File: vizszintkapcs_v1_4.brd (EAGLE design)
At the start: 235.7 x 107.2 mm, 95 parts, among them IC1 UA78M08DCY, IC2 7815TV, U1 MCP3004-I/ST

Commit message: smaller version with danger sign and good holes
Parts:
- moved WL4:OK3 34.8 mm to (159.8, 34.2)
- moved WL6:OK3 34.8 mm to (142.0, 34.2)
- moved WL3:OK3 34.8 mm to (168.7, 34.2)
- moved WL3:R9 34.8 mm to (167.4, 44.3)
- moved WL4:R9 34.8 mm to (158.6, 44.3)
- moved WL5:OK3 34.8 mm to (150.9, 34.2)
- moved WL5:R9 34.8 mm to (149.7, 44.3)
- moved WL6:R9 34.8 mm to (140.8, 44.3)
- moved WL4:R8 33.6 mm to (159.7, 26.8), turned to 0 degrees
- moved WL3:R8 33.6 mm to (168.6, 26.8), turned to 0 degrees
- moved WL5:R8 33.6 mm to (150.8, 26.8), turned to 0 degrees
- moved WL6:R8 33.6 mm to (141.9, 26.8), turned to 0 degrees
- moved U$6 33.0 mm to (165.1, 5.08)
- moved WL4:B3 32.1 mm to (159.7, 16.5)
- moved WL4:C4 32.1 mm to (159.7, 24.1)
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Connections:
- net 230V0: now also U$8.P$3@1, U$8.P$3@2; no longer U$8.P$3
- net 230VPHASE: now also U$8.P$1@1, U$8.P$1@2; no longer U$8.P$1
- net COMMON_EARTH: now also U$8.P$10@1, U$8.P$10@2, U$8.P$2@1, U$8.P$2@2, U$8.P$5@1, U$8.P$5@2, U$8.P$8@1, U$8.P$8@2; no longer U$8.P$10, U$8.P$2, U$8.P$5, U$8.P$8
- net MOTOR_IN: now also U$8.P$4@1, U$8.P$4@2; no longer U$8.P$4
- net MOTOR_IN_2: now also U$8.P$7@1, U$8.P$7@2; no longer U$8.P$7
- net MOTOR_OUT_1: now also U$8.P$6@1, U$8.P$6@2; no longer U$8.P$6
- net MOTOR_OUT_2: now also U$8.P$9@1, U$8.P$9@2; no longer U$8.P$9
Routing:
- net DC5V: track 415.8 -> 381.8 mm, vias 7 -> 6
- net MOTOR_IN: track 36.2 -> 66.4 mm
- net MOTOR_OUT_1: track 45.3 -> 73.4 mm
- net P1.6: track 86.9 -> 113.4 mm, vias 1 -> 4
- net MOTOR_IN_2: track 31.9 -> 58.3 mm
- net AC12V: track 114.4 -> 138.7 mm
- net DC15V: track 234.8 -> 212.1 mm
- net COMMON_EARTH: track 52.5 -> 73.6 mm
- net MOTOR_DIRECT_1: track 126.1 -> 108.4 mm
- net P6.1: track 115.9 -> 98.7 mm
- net DC8V: track 126.4 -> 142.0 mm, vias 3 -> 1
- net MOTOR_DIRECT_2: track 152.7 -> 138.5 mm
- net P6.0: track 138.9 -> 125.3 mm
- net 230V0: track 106.2 -> 117.5 mm, vias 1 -> 0
- net P2.7: track 161.4 -> 151.8 mm
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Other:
- board size 235.7 x 107.2 mm -> 197.6 x 97 mm
- board text added: "DANGER! HIGH VOLTAGE!"
- board text added: "High voltage"
- board text added: "Water Cleaning Management System (c) ujoimro, 2015-05-11 https://github.com/ViktorVaczi90/viztisztito"

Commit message: save
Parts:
- B2, B7: device rectifier:RB1A -> rectifier:1KAB
- C1, C10, C13, C2, C3, C5: device capacitor-wima:C2.5-3 -> adafruit:E3,5-8
- IC1: value UA78M08DCY -> UA78M33DCY
- moved C4 5.08 mm to (175.6, 57.0)
- moved C2 4.14 mm to (149.5, 51.1), turned to 270 degrees
- moved C10 3.81 mm to (145.8, 78.7)
- moved C1 2.54 mm to (170.2, 57.1)
- moved C3 2.54 mm to (149.9, 59.7)
- moved B2 2.54 mm to (132.1, 73.7), turned to 180 degrees
- moved C6 2.54 mm to (172.7, 71.1)
- moved C7 2.54 mm to (154.9, 54.6)
- moved C9 2.54 mm to (155.0, 59.8)
- moved IC2 2.54 mm to (154.9, 73.7)
- moved C12 1.27 mm to (140.5, 75.0)
- moved C5 1.27 mm to (166.4, 71.1)
- moved IC1 1.27 mm to (161.3, 55.9)
- moved U$2 1.27 mm to (161.3, 73.7)
- moved C14 1.21 mm to (140.5, 69.8), turned to 90 degrees
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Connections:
- net DC15V: now also C13.+; no longer C13.1
- net DC3.3V: now also C1.+; no longer C1.1
- net DC5V: now also C3.+; no longer C3.1
- net DC8V: now also C5.+; no longer C5.1
- net GND: now also C1.-, C10.-, C13.-, C2.-, C3.-, C5.-; no longer C1.2, C10.2, C13.2, C2.2, C3.2, C5.2
- net REC12V: now also C2.+; no longer C2.1
- net REC24V: now also C10.+; no longer C10.1
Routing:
- net REC24V: track 27.7 -> 38.2 mm
- net GND: track 164.6 -> 154.4 mm
- net REC12V: track 28.1 -> 35.8 mm
- net DC8V: track 142.0 -> 144.8 mm
- net TRANS_OUT: track 170.9 -> 168.3 mm, vias 2 -> 3
- net DC15V: track 212.1 -> 214.1 mm
- net DC5V: track 381.8 -> 380.0 mm
- net AC24V: track 25.3 -> 23.5 mm
- net DC3.3V: track 74.6 -> 76.1 mm

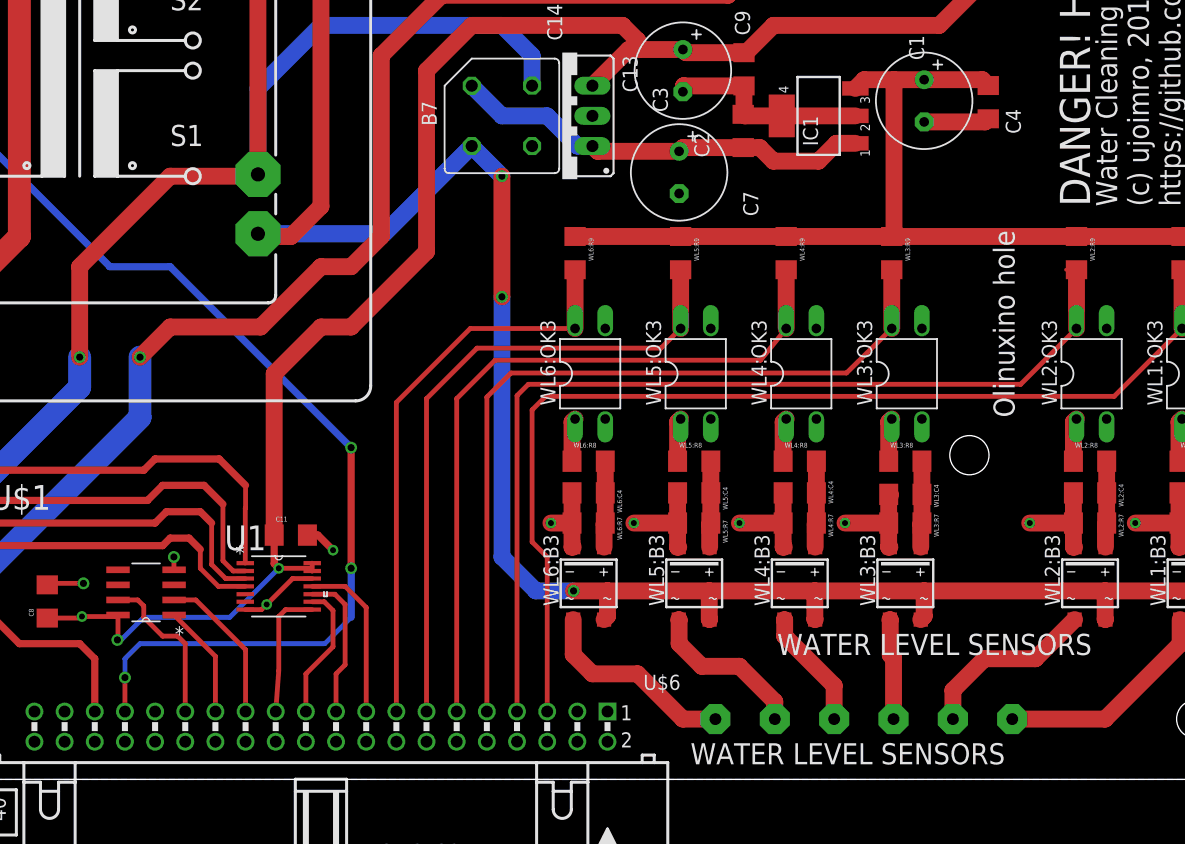
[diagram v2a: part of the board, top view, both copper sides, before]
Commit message: only 4 water level sensor on one board
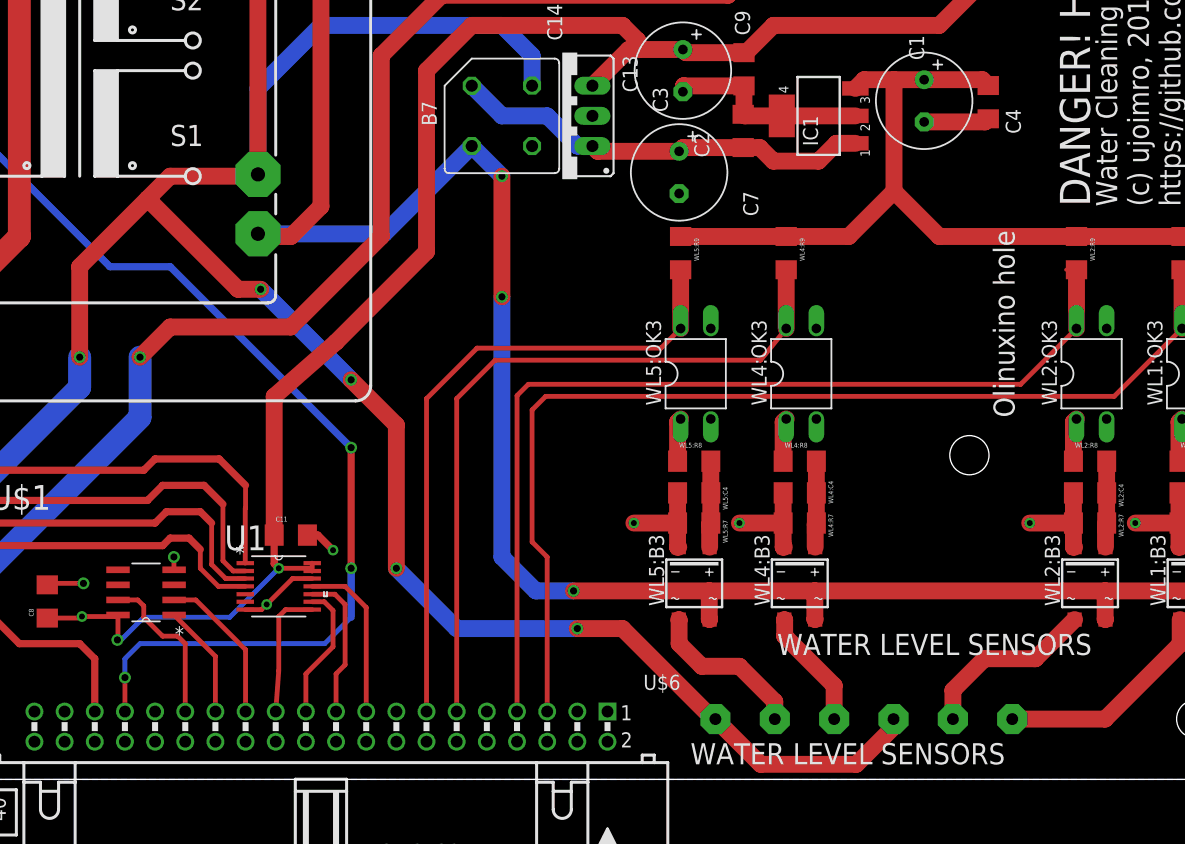
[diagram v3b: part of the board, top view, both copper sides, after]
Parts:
- removed WL3:B3, WL6:B3: MB6S, rectifier:SOIC-4
- removed WL3:C4, WL6:C4: 10uF, SparkFun-Passives:1206
- removed WL3:OK3, WL6:OK3: PC817, optocoupler:DIL04
- removed WL3:R7, WL6:R7: 20k, SparkFun-Resistors:1206
- removed WL3:R8, WL3:R9, WL6:R8, WL6:R9: 2k, SparkFun-Resistors:1206
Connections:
- removed net 3_WATER_IN: U$6.P$3, WL3:B3.~1
- removed net 6_WATER_IN: U$6.P$6, WL6:B3.~1
- removed net WL3:N$12: WL3:B3.+, WL3:C4.1, WL3:R7.2, WL3:R8.2
- removed net WL3:N$13: WL3:OK3.1, WL3:R8.1
- removed net WL6:N$12: WL6:B3.+, WL6:C4.1, WL6:R7.2, WL6:R8.2
- removed net WL6:N$13: WL6:OK3.1, WL6:R8.1
- net AC12V: now also U$6.P$3, U$6.P$6
- net DC3.3V: no longer WL3:R9.1, WL6:R9.1
- net GND: no longer WL3:B3.-, WL3:C4.2, WL3:OK3.2, WL3:OK3.3, WL3:R7.1, WL6:B3.-, WL6:C4.2, WL6:OK3.2, WL6:OK3.3, WL6:R7.1
- net P1.4: no longer WL3:OK3.4, WL3:R9.2
- net P2.5: no longer WL6:OK3.4, WL6:R9.2
- net TRANS_OUT: no longer WL3:B3.~2, WL6:B3.~2
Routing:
- net AC12V: track 138.7 -> 230.3 mm, vias 1 -> 5
- net P1.4: track 67.9 -> 0.00 mm
- net P2.5: track 48.6 -> 0.00 mm
- net 6_WATER_IN: track 17.2 -> 0.00 mm
- net GND: track 154.4 -> 139.5 mm, vias 16 -> 14
- net DC3.3V: track 76.1 -> 66.5 mm
- net 3_WATER_IN: track 8.51 -> 0.00 mm
- net WL3:N$12: track 7.28 -> 0.00 mm
- net WL6:N$12: track 7.28 -> 0.00 mm
- net TRANS_OUT: track 168.3 -> 163.3 mm
- net WL6:N$13: track 3.66 -> 0.00 mm
- net WL3:N$13: track 3.66 -> 0.00 mm
- net DC5V: track 380.0 -> 378.7 mm

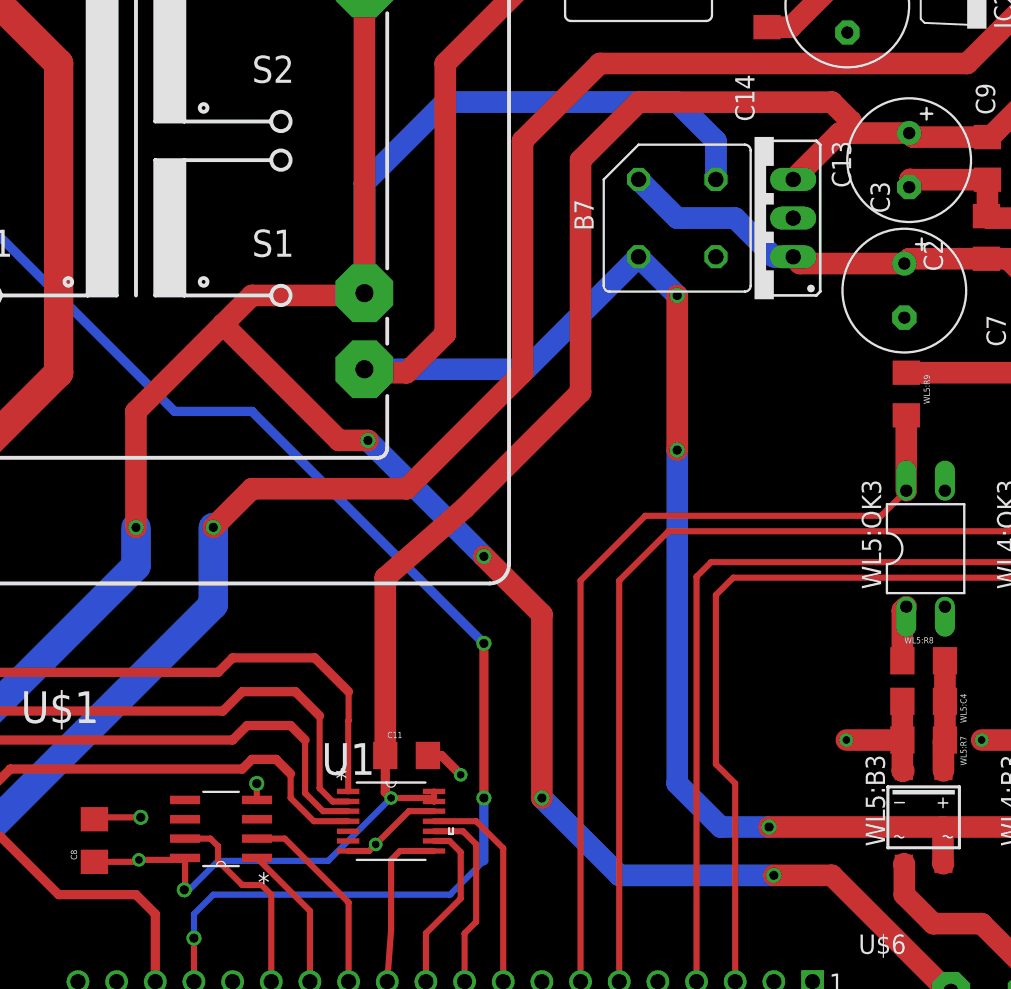
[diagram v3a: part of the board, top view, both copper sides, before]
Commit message: 3.3v spi levels
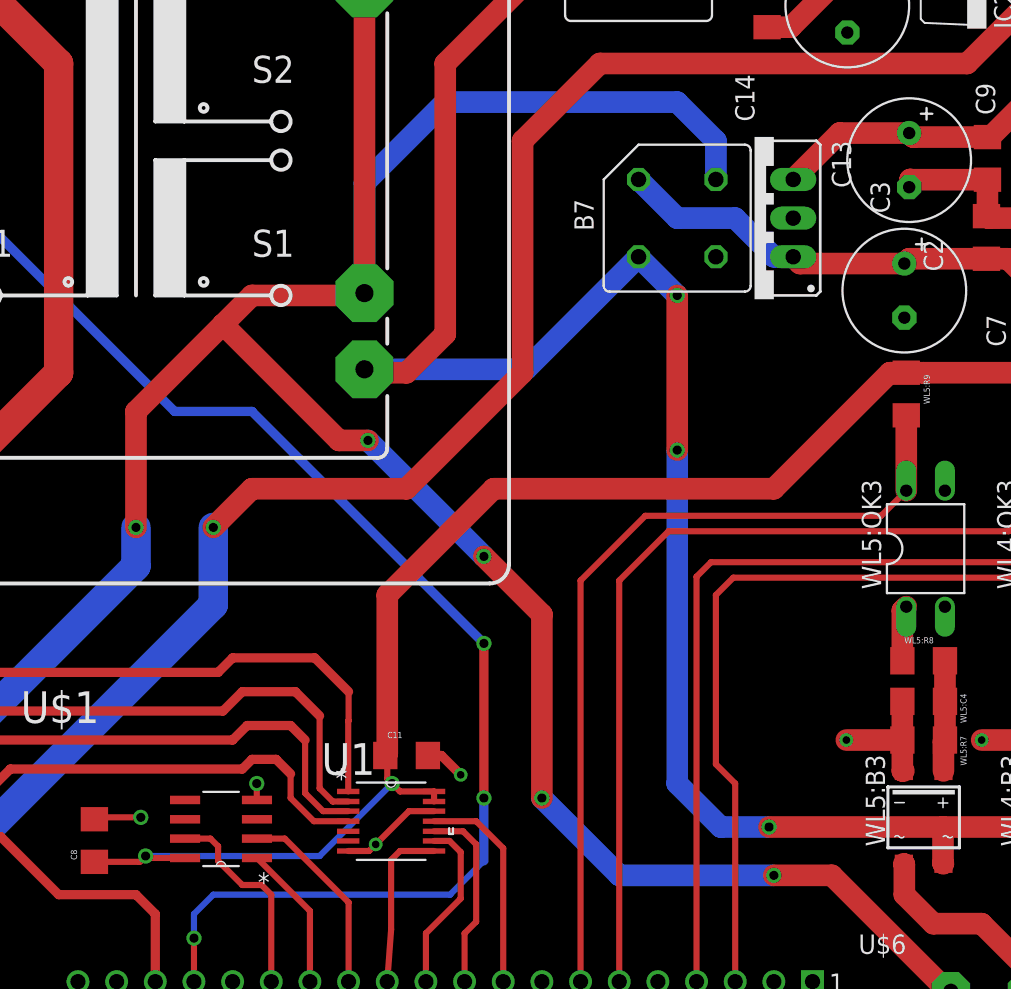
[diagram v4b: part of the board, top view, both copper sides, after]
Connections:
- net DC3.3V: now also C11.1, C8.1, U$1.8, U1.13, U1.14
- net DC5V: no longer C11.1, C8.1, U$1.8, U1.13, U1.14
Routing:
- net DC5V: track 378.7 -> 282.6 mm, vias 6 -> 3
- net DC3.3V: track 66.5 -> 147.2 mm, vias 0 -> 2
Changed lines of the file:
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@@
 <wire x1="13.332" y1="63.0398" x2="12.7762" y2="62.484" width="0.6096" layer="1"/>
 <wire x1="13.332" y1="65.408" x2="13.332" y2="66.802" width="1.4224" layer="1"/>
-<contactref element="U1" pad="14"/>
-<contactref element="U1" pad="13"/>
-<contactref element="C8" pad="1"/>
-<contactref element="C11" pad="1"/>
-<contactref element="U$1" pad="8"/>
-<wire x1="102.2858" y1="13.843" x2="102.1588" y2="13.716" width="0.4064" layer="1"/>
-<wire x1="102.1588" y1="13.716" x2="99.2505" y2="13.716" width="0.4064" layer="1"/>
-<wire x1="118.6434" y1="17.5514" x2="118.6434" y2="18.2118" width="0.4064" layer="1"/>
-<wire x1="118.6434" y1="17.5514" x2="118.4148" y2="17.78" width="0.4064" layer="1"/>
-<wire x1="118.4148" y1="17.78" x2="115.824" y2="17.78" width="0.4064" layer="1"/>
-<via x="115.824" y="17.78" extent="1-16" drill="0.5" shape="octagon"/>
-<wire x1="115.824" y1="17.78" x2="111.6965" y2="13.6525" width="0.4064" layer="16"/>
-<via x="99.2505" y="13.716" extent="1-16" drill="0.5" shape="octagon"/>
 <contactref element="SSR_MOT:200" pad="1"/>
-<wire x1="115.44" y1="20.574" x2="115.44" y2="18.164" width="0.6096" layer="1"/>
-<wire x1="115.44" y1="18.164" x2="115.824" y2="17.78" width="0.6096" layer="1"/>
 <contactref element="REL_MOT:200" pad="1"/>
 <contactref element="C3" pad="+"/>
@@
 <wire x1="15.24" y1="71.12" x2="13.332" y2="69.212" width="1.4224" layer="1"/>
 <wire x1="13.332" y1="69.212" x2="13.332" y2="66.802" width="1.4224" layer="1"/>
-<wire x1="115.44" y1="32.255" x2="115.44" y2="20.574" width="1.4224" layer="1"/>
 <wire x1="51.4066" y1="62.8874" x2="50.8762" y2="62.357" width="0.6096" layer="1"/>
-<wire x1="120.65" y1="36.83" x2="115.44" y2="32.255" width="1.4224" layer="1"/>
-<wire x1="144.78" y1="63.5" x2="132.08" y2="63.5" width="1.4224" layer="1"/>
-<wire x1="132.08" y1="63.5" x2="128.27" y2="59.69" width="1.4224" layer="1"/>
-<wire x1="111.6965" y1="13.6525" x2="104.4575" y2="13.6525" width="0.4064" layer="16"/>
-<wire x1="104.4575" y1="13.6525" x2="102.5525" y2="11.7475" width="0.4064" layer="16"/>
-<wire x1="102.5525" y1="11.7475" x2="102.235" y2="11.7475" width="0.4064" layer="16"/>
-<via x="102.235" y="11.7475" extent="1-16" drill="0.6" shape="octagon"/>
-<wire x1="102.235" y1="11.7475" x2="102.2858" y2="11.7983" width="0.4064" layer="1"/>
-<wire x1="102.2858" y1="11.7983" x2="102.2858" y2="13.843" width="0.4064" layer="1"/>
-<wire x1="99.2505" y1="13.716" x2="99.1205" y2="13.586" width="0.4064" layer="1"/>
-<wire x1="99.1205" y1="13.586" x2="96.3295" y2="13.586" width="0.4064" layer="1"/>
 <via x="55.88" y="86.36" extent="1-16" drill="0.6" shape="octagon"/>
 <wire x1="163.83" y1="88.9" x2="176.53" y2="76.2" width="1.4224" layer="1"/>
@@
 <wire x1="35.56" y1="86.49" x2="28.07" y2="86.49" width="1.4224" layer="1"/>
 <wire x1="28.07" y1="86.49" x2="27.94" y2="86.36" width="1.4224" layer="1"/>
-<wire x1="120.65" y1="36.83" x2="128.27" y2="44.45" width="1.4224" layer="1"/>
-<wire x1="128.27" y1="44.45" x2="128.27" y2="59.69" width="1.4224" layer="1"/>
 <wire x1="142.24" y1="58.42" x2="145.288" y2="61.468" width="1.4224" layer="1"/>
-<wire x1="145.288" y1="61.468" x2="146.05" y2="61.468" width="1.4224" layer="1"/>
-<wire x1="146.05" y1="61.468" x2="149.86" y2="61.468" width="1.4224" layer="1"/>
-<wire x1="144.78" y1="63.5" x2="146.05" y2="62.23" width="1.4224" layer="1"/>
-<wire x1="146.05" y1="62.23" x2="146.05" y2="61.468" width="1.4224" layer="1"/>
+<wire x1="145.288" y1="61.468" x2="149.86" y2="61.468" width="1.4224" layer="1"/>
 <wire x1="149.86" y1="61.468" x2="150.1237" y2="61.2043" width="1.4224" layer="1"/>
 <wire x1="150.1237" y1="61.2043" x2="155.0035" y2="61.2043" width="1.4224" layer="1"/>
@@
 <wire x1="183.007" y1="45.723" x2="171.447" y2="45.723" width="1.4224" layer="1"/>
 <wire x1="171.447" y1="45.723" x2="167.64" y2="49.53" width="1.4224" layer="1"/>
+<contactref element="U1" pad="13"/>
+<contactref element="C8" pad="1"/>
+<contactref element="U1" pad="14"/>
+<contactref element="C11" pad="1"/>
+<contactref element="U$1" pad="8"/>
+<wire x1="149.6695" y1="45.723" x2="148.593" y2="45.723" width="1.4224" layer="1"/>
+<wire x1="148.593" y1="45.723" x2="140.97" y2="38.1" width="1.4224" layer="1"/>
+<wire x1="140.97" y1="38.1" x2="122.555" y2="38.1" width="1.4224" layer="1"/>
+<wire x1="122.555" y1="38.1" x2="115.57" y2="31.115" width="1.4224" layer="1"/>
+<wire x1="115.57" y1="31.115" x2="115.57" y2="20.704" width="1.4224" layer="1"/>
+<wire x1="115.57" y1="20.704" x2="115.44" y2="20.574" width="1.4224" layer="1"/>
+<wire x1="118.6434" y1="18.2118" x2="116.4082" y2="18.2118" width="0.4064" layer="1"/>
+<wire x1="116.4082" y1="18.2118" x2="115.8875" y2="18.7325" width="0.4064" layer="1"/>
+<wire x1="115.8875" y1="18.7325" x2="115.57" y2="19.05" width="0.4064" layer="1"/>
+<wire x1="115.57" y1="19.05" x2="115.57" y2="20.444" width="0.4064" layer="1"/>
+<wire x1="115.57" y1="20.444" x2="115.44" y2="20.574" width="0.4064" layer="1"/>
+<wire x1="118.6434" y1="18.2118" x2="118.6434" y2="17.5514" width="0.4064" layer="1"/>
+<wire x1="96.3295" y1="13.586" x2="99.311" y2="13.586" width="0.4064" layer="1"/>
+<wire x1="99.311" y1="13.586" x2="99.695" y2="13.97" width="0.4064" layer="1"/>
+<via x="99.695" y="13.97" extent="1-16" drill="0.6" shape="octagon"/>
+<wire x1="99.695" y1="13.97" x2="111.125" y2="13.97" width="0.4064" layer="16"/>
+<wire x1="111.125" y1="13.97" x2="115.8875" y2="18.7325" width="0.4064" layer="16"/>
+<via x="115.8875" y="18.7325" extent="1-16" drill="0.6" shape="octagon"/>
+<wire x1="99.695" y1="13.97" x2="99.822" y2="13.843" width="0.4064" layer="1"/>
+<wire x1="99.822" y1="13.843" x2="102.2858" y2="13.843" width="0.4064" layer="1"/>
 </signal>
 <signal name="USB-SERIAL2:VCCIO">
